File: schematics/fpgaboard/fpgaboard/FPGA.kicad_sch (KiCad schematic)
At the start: 15 parts, among them J1 SODIMM-200, U1 LFE5UM-85F-8BG381I, U13 W25Q32JVSS

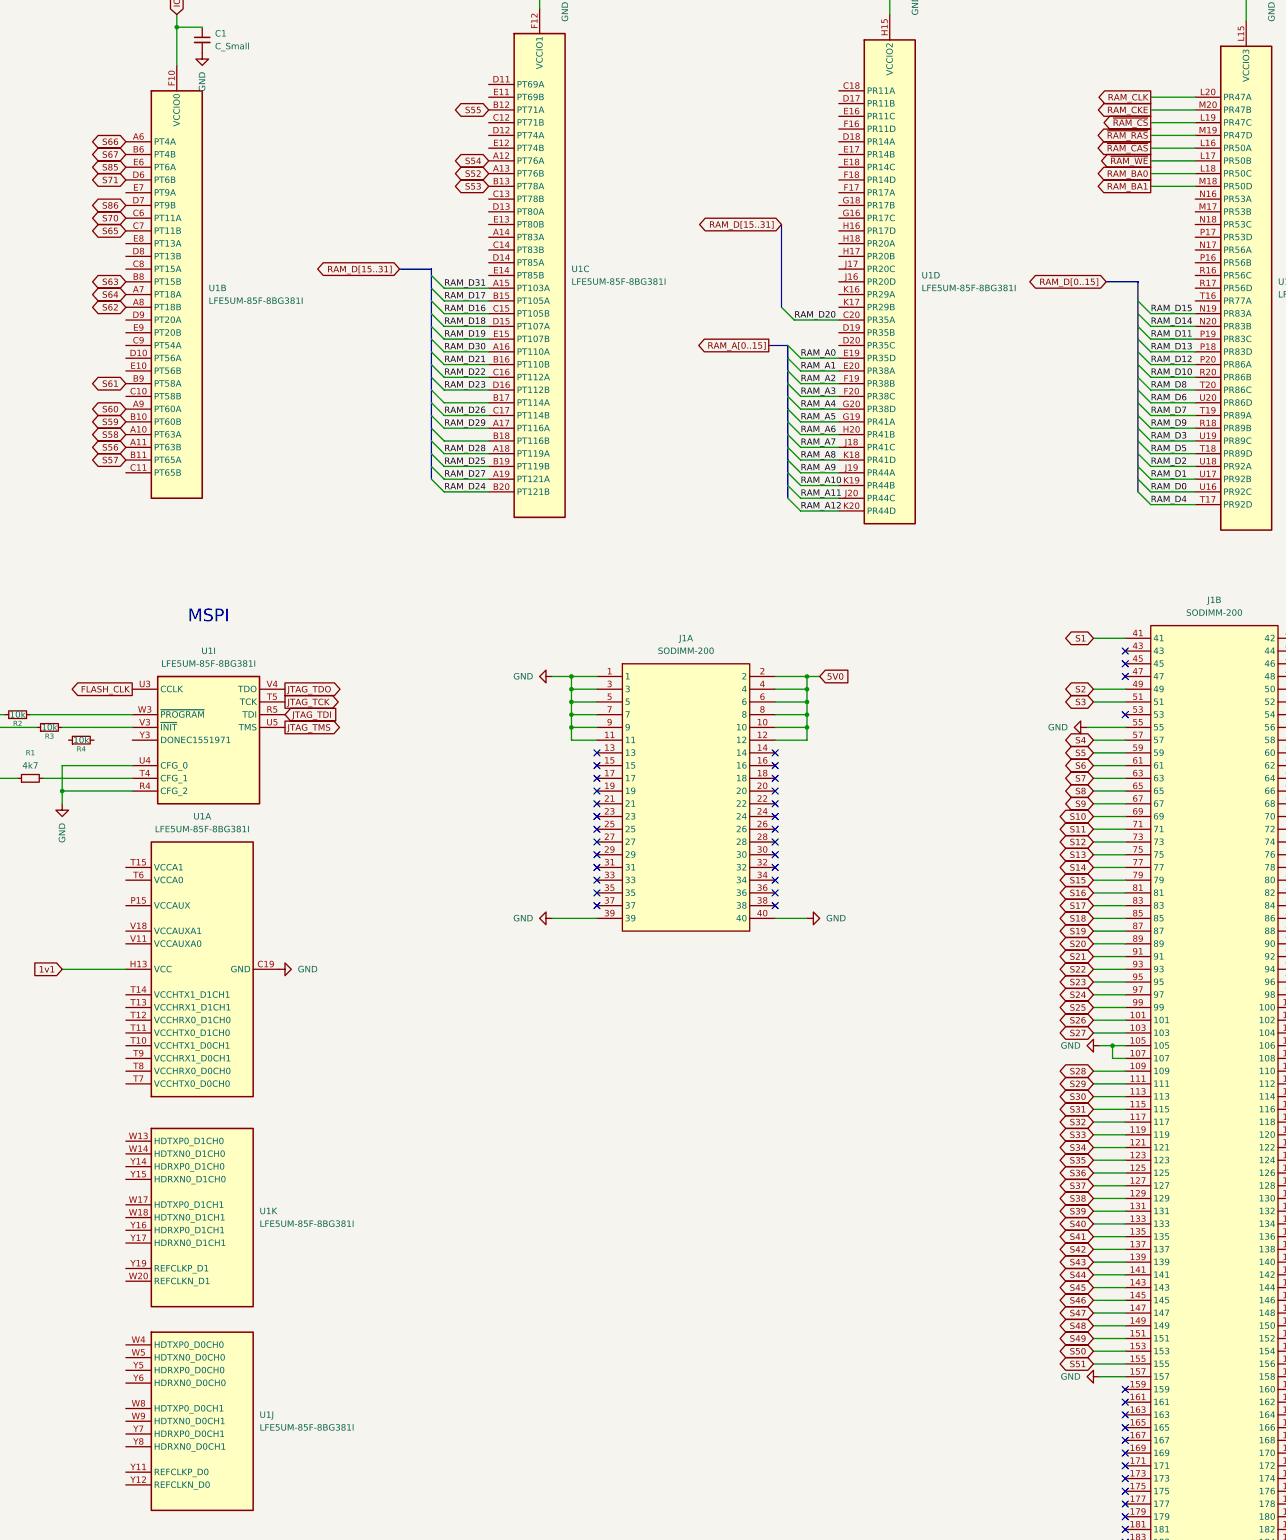
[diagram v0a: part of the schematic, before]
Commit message: SODIMM connector fully wired up to FPGA.
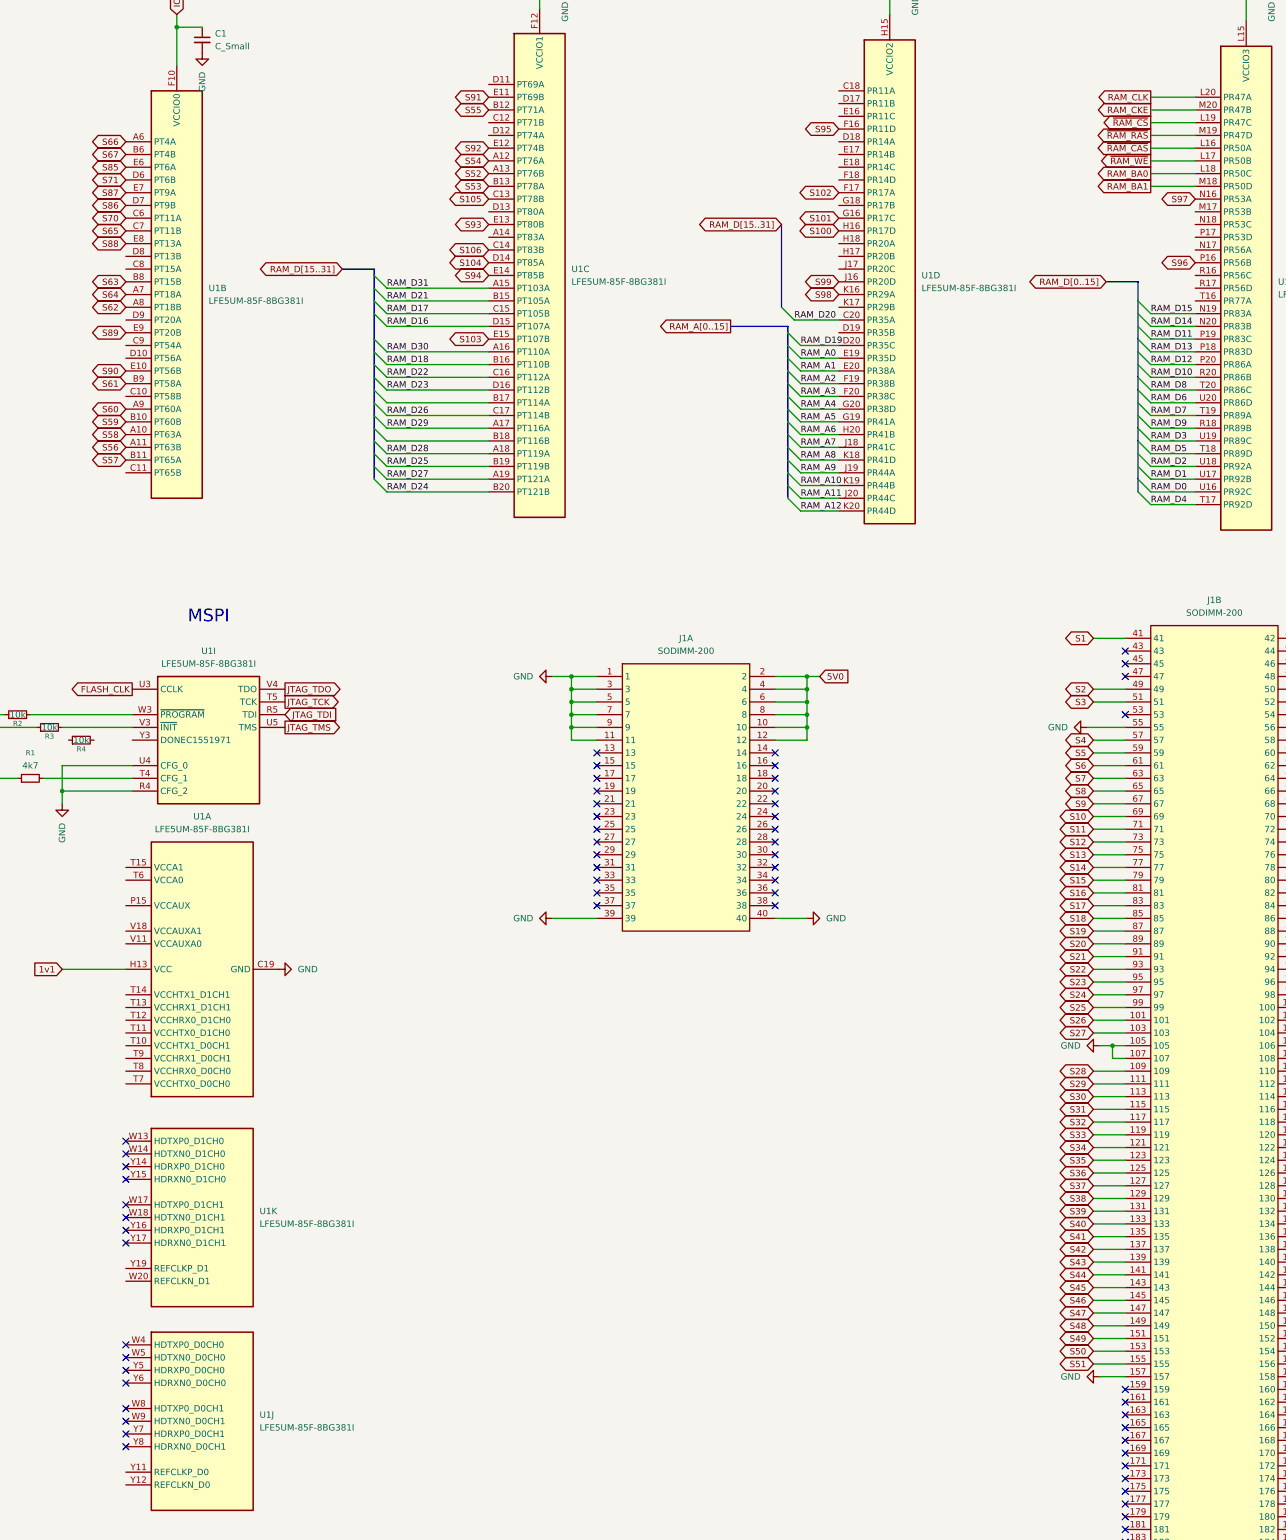
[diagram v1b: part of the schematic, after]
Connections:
- net RAM_D16: now also U1.D15 (PT107A); no longer U1.C15 (PT105B)
- net RAM_D17: now also U1.C15 (PT105B); no longer U1.B15 (PT105A)
- net RAM_D18: now also U1.B16 (PT110B); no longer U1.D15 (PT107A)
- net RAM_D19: now also U1.D20 (PR35C); no longer U1.E15 (PT107B)
- net RAM_D21: now also U1.B15 (PT105A); no longer U1.B16 (PT110B)
- net S100: now also U1.H16 (PR17D)
- net S101: now also U1.G16 (PR17C)
- net S102: now also U1.F17 (PR17A)
- net S103: now also U1.E15 (PT107B)
- net S104: now also U1.D14 (PT85A)
- net S105: now also U1.C13 (PT78B)
- net S106: now also U1.C14 (PT83B)
- net S87: now also U1.E7 (PT9A)
- net S88: now also U1.E8 (PT13A)
- net S89: now also U1.E9 (PT20B)
- net S90: now also U1.E10 (PT56B)
- net S91: now also U1.E11 (PT69B)
- net S92: now also U1.E12 (PT74B)
- net S93: now also U1.E13 (PT80B)
- net S94: now also U1.E14 (PT85B)
- net S95: now also U1.F16 (PR11D)
- net S96: now also U1.P16 (PR56B)
- net S97: now also U1.N16 (PR53A)
- net S98: now also U1.K16 (PR29A)
- net S99: now also U1.J16 (PR20D)
- no-connect marks 70 -> 86

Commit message: Work on connecting up SDRAM to FPGA.
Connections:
- net RAM_A0: now also U1.R17 (PR56D); no longer U1.E19 (PR35D)
- net RAM_A10: now also U1.P17 (PR53D); no longer U1.K19 (PR44B)
- net RAM_A4: now also U1.C16 (PT112A)
- net RAM_A5: now also U1.C17 (PT114B)
- net RAM_A6: now also U1.D16 (PT112B)
- net RAM_BA0: now also U1.M17 (PR53B); no longer U1.L18 (PR50C)
- net RAM_BA1: now also U1.N17 (PR56A); no longer U1.M18 (PR50D)
- net RAM_D18: now also U1.C20 (PR35A); no longer U1.B16 (PT110B)
- net RAM_D19: now also U1.B18 (PT116B); no longer U1.D20 (PR35C)
- net RAM_D20: now also U1.B17 (PT114A); no longer U1.C20 (PR35A)
- net RAM_D21: now also U1.B16 (PT110B); no longer U1.B15 (PT105A)
- net RAM_D22: now also U1.B15 (PT105A); no longer U1.C16 (PT112A)
- net RAM_D23: no longer U1.D16 (PT112B)
- net RAM_D25: no longer U1.B19 (PT119B)
- net RAM_D26: no longer U1.C17 (PT114B)
- net ~{RAM_CS}: now also U1.M18 (PR50D); no longer U1.L19 (PR47C)
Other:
- note added: "- Wire middle of BGA pads - Via shortcut other tracks - All RAM pins connected, no dups or missing."
- moved on the sheet: C4, U1E
